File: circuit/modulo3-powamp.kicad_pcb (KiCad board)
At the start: 2 copper layers, 105 x 47 mm, 60 parts, among them J1 HOLE, J2 HOLE, J3 HOLE, J4 HOLE, J5 CONN_01X04, Q1 BS170, SW1 reset, SW3 HEAD/AD, U2 TPA3220, U5 PWR_CONN, U6 AMPCTRL

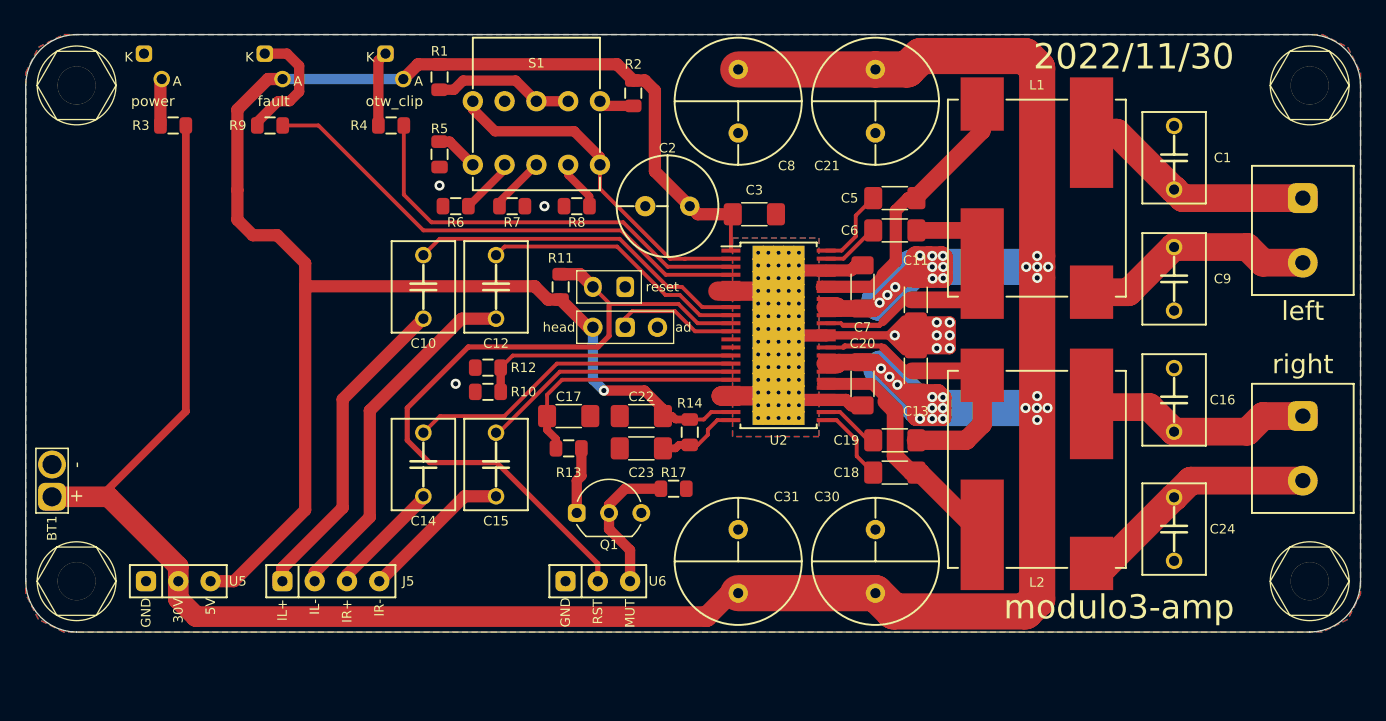
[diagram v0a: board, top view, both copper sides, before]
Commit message: added ampctrl and diffaudio; started changing powamp
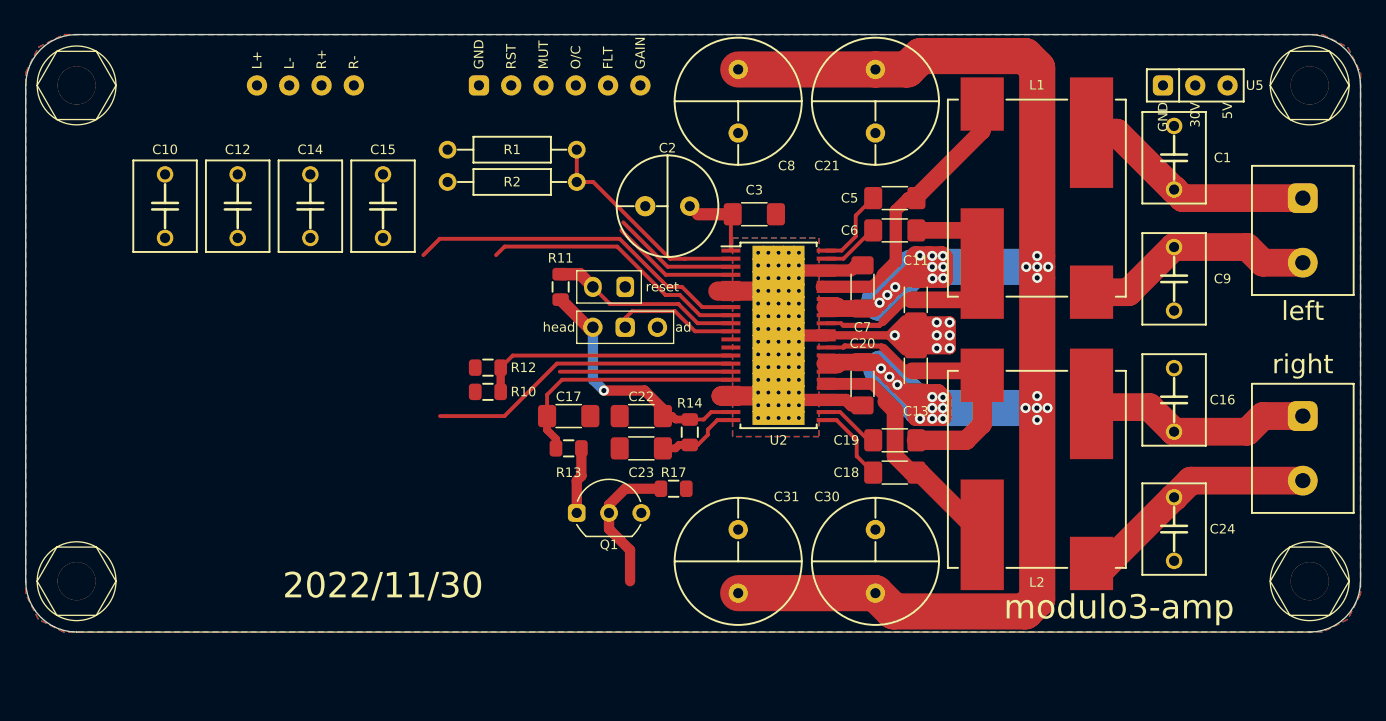
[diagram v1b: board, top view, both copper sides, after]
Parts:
- removed BT1: BATT, myAmp:BATTERY
- removed D1: power, myAmp:LED_D3.0mm_PCBedge
- removed D2: otw_clip, myAmp:LED_D3.0mm_PCBedge
- removed D3: fault, myAmp:LED_D3.0mm_PCBedge
- removed J5: CONN_01X04, myAmp:PIN_1x04
- removed R3: 10K, myAmp:R_0805
- removed R4, R9: 1K, myAmp:R_0805
- removed R5: 5K6, myAmp:R_0805
- removed R6: 20K, myAmp:R_0805
- removed R7: 39K, myAmp:R_0805
- removed R8: 47K, myAmp:R_0805
- removed S1: GAINSEL, myAmp:SR10010F-0204
- added U1: DIFFAUDIO, myAmp:DIFFAUDIO, F.Cu at (72.0, 54.0)
- R1: footprint myAmp:R_0805 -> myAmp:R_10MM
- R2: value 75K -> 5K6; footprint myAmp:R_0805 -> myAmp:R_10MM
- U6: footprint myAmp:PIN_1x03 -> myAmp:AMPCTRL
- moved U5 89.0 mm to (142.0, 54.0)
- moved U6 39.1 mm to (92.0, 54.0)
- moved C14 22.2 mm to (72.4, 63.5), turned to -90 degrees
- moved C15 22.2 mm to (78.1, 63.5), turned to -90 degrees
- moved C12 21.3 mm to (66.7, 63.5), turned to -90 degrees
- moved C10 21.3 mm to (61.0, 63.5), turned to -90 degrees
- moved R2 11.8 mm to (88.3, 61.6), turned to 0 degrees
- moved R1 8.08 mm to (88.3, 59.1), turned to 180 degrees
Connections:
- R1 pad 1: +5V -> GAIN_SLV
- R1 pad 2: Net-(R1-Pad2) -> +5V
- R2 pad 1: +5V -> GND
- R2 pad 2: Net-(R2-Pad2) -> GAIN_SLV
- U2 pad 2: Net-(S1-Pad1) -> GAIN_SLV
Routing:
- net +5V: track 137.4 -> 25.9 mm
- net +BATT: track 254.6 -> 161.8 mm
- net /RESET: track 58.6 -> 15.0 mm
- net FAULT: track 40.1 -> 10.1 mm
- net Net-(C12-Pad1): track 28.1 -> 0.00 mm
- net Net-(S1-Pad1): track 27.3 -> 0.00 mm
- net Net-(C10-Pad1): track 25.2 -> 0.00 mm
- net OTW_CLIP: track 33.5 -> 9.91 mm
- net GAIN_SLV: track 0.00 -> 17.2 mm
- net Net-(C15-Pad1): track 12.0 -> 0.00 mm
- net Net-(R1-Pad2): track 11.1 -> 0.00 mm
- net Net-(D3-Pad1): track 9.69 -> 0.00 mm
- net Net-(C14-Pad1): track 9.17 -> 0.00 mm
- net Net-(C15-Pad2): track 20.5 -> 13.5 mm
- net Net-(D2-Pad1): track 5.88 -> 0.00 mm
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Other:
- board text removed: "GND"
- board text removed: "IL+"
- board text removed: "IL-"
- board text removed: "IR+"
- board text removed: "IR-"
- board text removed: "MUT"
- board text removed: "RST"

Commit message: got the pcs and holes sizes for mcu, poweamp and fv1
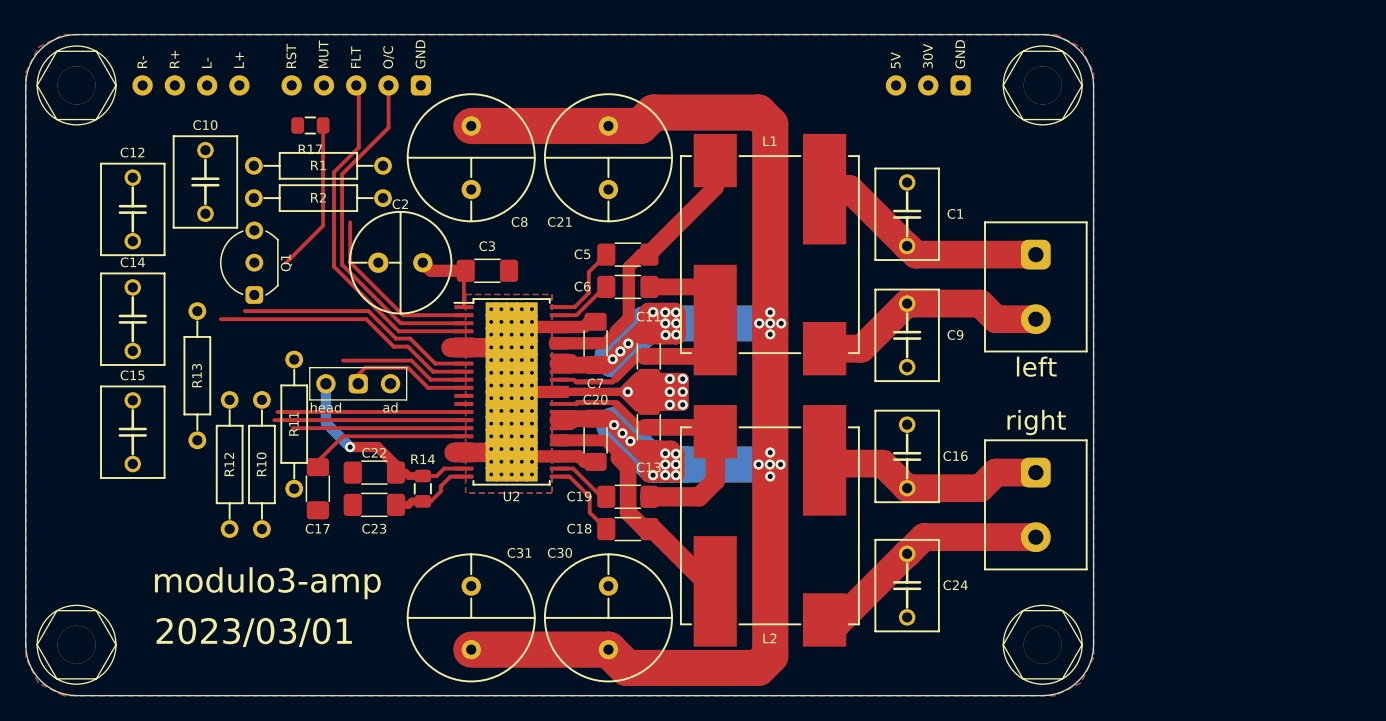
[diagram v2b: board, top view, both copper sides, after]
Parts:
- removed SW1: reset, myAmp:Switch_2.5mm
- R1: value 100K -> open
- R10, R11, R12, R13: footprint myAmp:R_0805 -> myAmp:R_10MM
- moved J2 48.8 mm to (130.0, 98.0)
- moved J1 44.3 mm to (130.0, 54.0)
- moved R17 40.4 mm to (72.4, 57.1), turned to 180 degrees
- moved Q1 34.1 mm to (68.0, 67.9), turned to 90 degrees
- moved R13 29.8 mm to (63.5, 76.8), turned to 90 degrees
- moved C15 26.5 mm to (58.4, 81.3)
- moved R11 23.6 mm to (71.1, 80.6)
- moved R12 21.7 mm to (66.0, 83.8), turned to 90 degrees
- moved C1 21.5 mm to (119.3, 64.1)
- moved C16 21.5 mm to (119.3, 83.2)
- moved C24 21.5 mm to (119.3, 93.3)
- moved C9 21.5 mm to (119.3, 73.7)
- moved C11 21.5 mm to (99.0, 75.3)
- moved C13 21.5 mm to (99.0, 80.9)
- moved C18 21.5 mm to (97.4, 88.9)
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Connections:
- U6 pad 4: OTW_CLIP -> FAULT
- U6 pad 5: FAULT -> OTW_CLIP
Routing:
- net FAULT: track 10.1 -> 27.5 mm
- net OTW_CLIP: track 9.91 -> 27.1 mm
- net Net-(C14-Pad2): track 24.6 -> 14.9 mm
- net Net-(C10-Pad2): track 26.9 -> 19.0 mm
- net /CMUTE: track 19.5 -> 12.8 mm
- net /FREQ_ADJ: track 20.4 -> 14.7 mm
- net Net-(Q1-Pad1): track 5.23 -> 0.00 mm
- net /RESET: track 15.0 -> 10.1 mm
- net GAIN_SLV: track 17.2 -> 13.8 mm
- net +5V: track 25.9 -> 22.8 mm
- net Net-(Q1-Pad2): track 11.3 -> 12.0 mm
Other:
- board size 105 x 47 mm -> 84 x 52 mm
- board text added: "2023/03/01"
- board text removed: "2022/11/30"

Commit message: fv-1 mostly done; power progressed
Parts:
- moved SPK1 0.08 mm to (129.5, 69.8)
- moved SPK2 0.08 mm to (129.5, 87.0)
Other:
- board text removed: "min 4Ω"

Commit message: lotsa things :)
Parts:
- removed Q1: BS170, myAmp:TO-92_Inline_Wide
- removed R17: 47K, myAmp:R_0805
- moved R10 4.49 mm to (65.4, 80.6)
- moved R13 4.49 mm to (67.9, 77.5)
- moved R12 4.40 mm to (63.0, 80.6)
- moved C17 1.91 mm to (73.0, 83.8)
- moved C3 0.64 mm to (86.4, 69.2)
- moved R11 0.64 mm to (70.5, 80.6)
- moved C12 0.25 mm to (58.4, 63.5)
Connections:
- R13 pad 2: Net-(Q1-Pad1) -> /MUTE
- U6 pad 3: Net-(Q1-Pad2) -> /MUTE
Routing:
- net +5V: track 22.8 -> 128.5 mm, vias 1 -> 2
- net /RESET: track 10.1 -> 53.3 mm
- net Net-(U1-R-): track 0.00 -> 27.5 mm
- net /MUTE: track 0.00 -> 23.1 mm
- net Net-(U1-R+): track 0.00 -> 19.0 mm
- net +BATT: track 161.8 -> 177.4 mm
- net Net-(U2-IN2_M): track 13.5 -> 27.2 mm
- net Net-(U2-IN2_P): track 14.9 -> 28.3 mm
- net Net-(Q1-Pad2): track 12.0 -> 0.00 mm
- net Net-(U2-IN1_M): track 20.8 -> 32.1 mm
- net Net-(U1-L-): track 0.00 -> 10.1 mm
- net Net-(U2-IN1_P): track 19.0 -> 29.0 mm
- net /FREQ_ADJ: track 14.7 -> 23.1 mm
- net Net-(U1-L+): track 0.00 -> 6.20 mm
- net /CMUTE: track 12.8 -> 16.9 mm
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
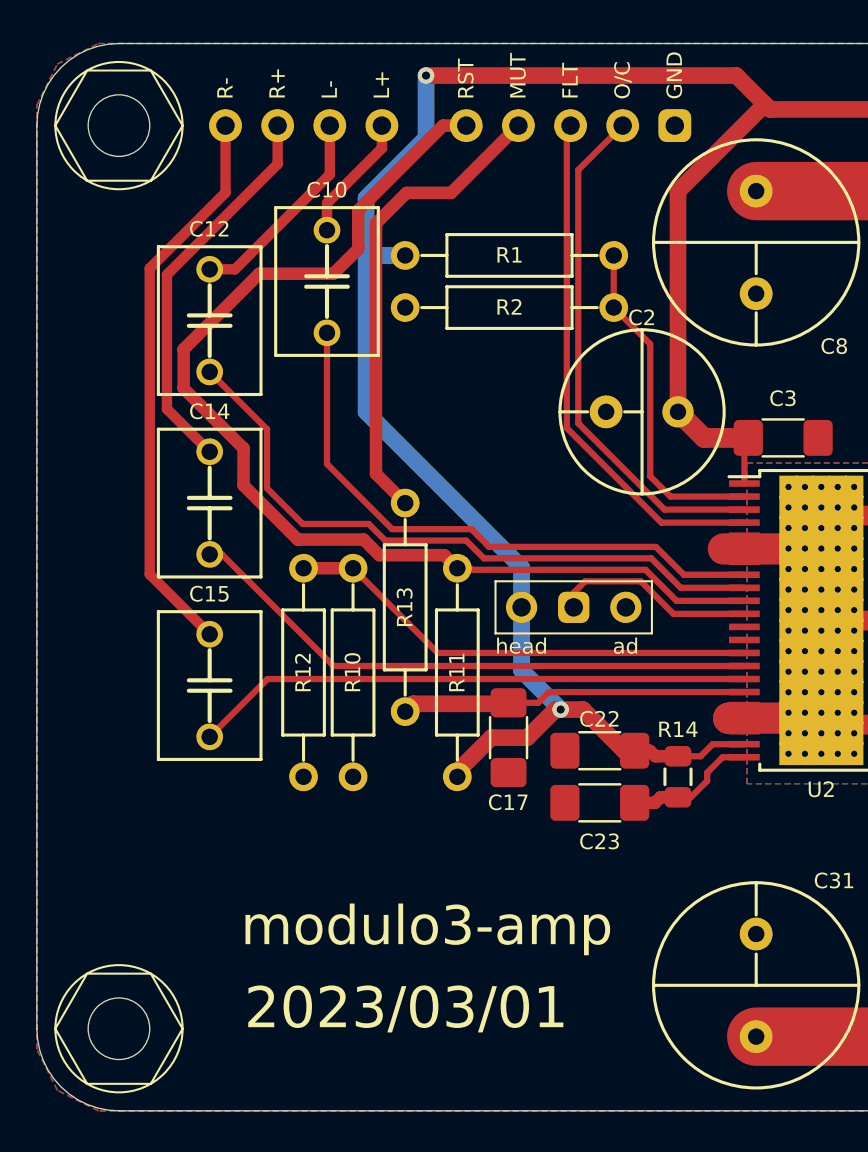
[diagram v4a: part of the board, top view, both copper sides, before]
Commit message: tweaked power amp and fv1
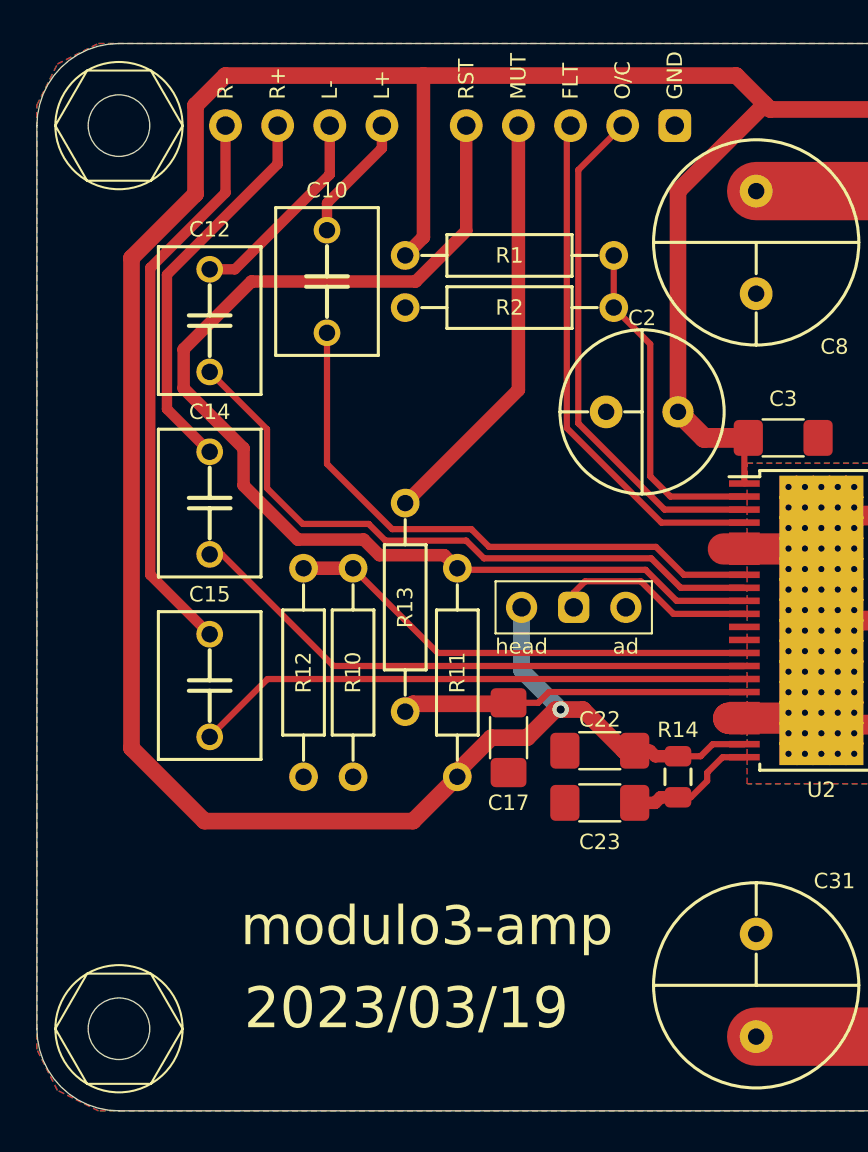
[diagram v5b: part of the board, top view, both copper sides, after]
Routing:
- net +5V: track 128.5 -> 168.2 mm, vias 2 -> 1
- net /RESET: track 53.3 -> 55.9 mm
- net /MUTE: track 23.1 -> 20.7 mm
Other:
- board text added: "2023/03/19"
- board text removed: "2023/03/01"
